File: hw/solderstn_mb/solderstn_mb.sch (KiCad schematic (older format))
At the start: 0 parts

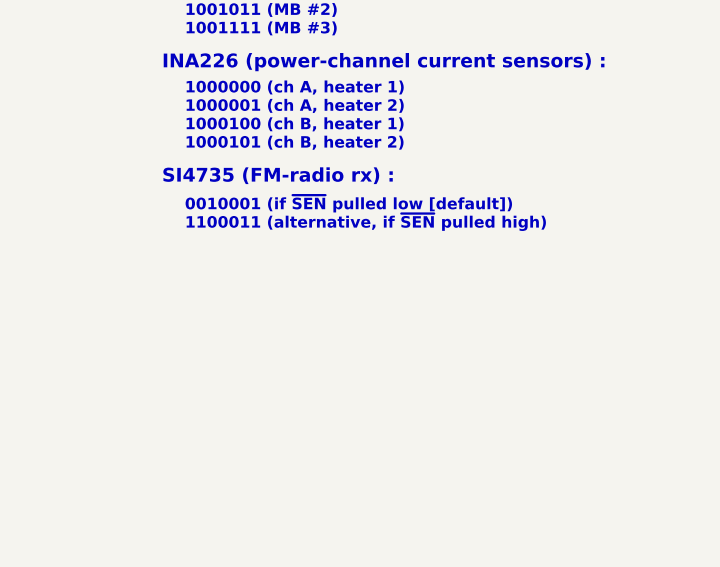
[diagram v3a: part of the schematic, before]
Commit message: Pinout changes to add DS3231 RTC module instead of 32kHz LSE xtal (still keep SMD pads as placeholders). Minor ERC fixes. All footprints specified
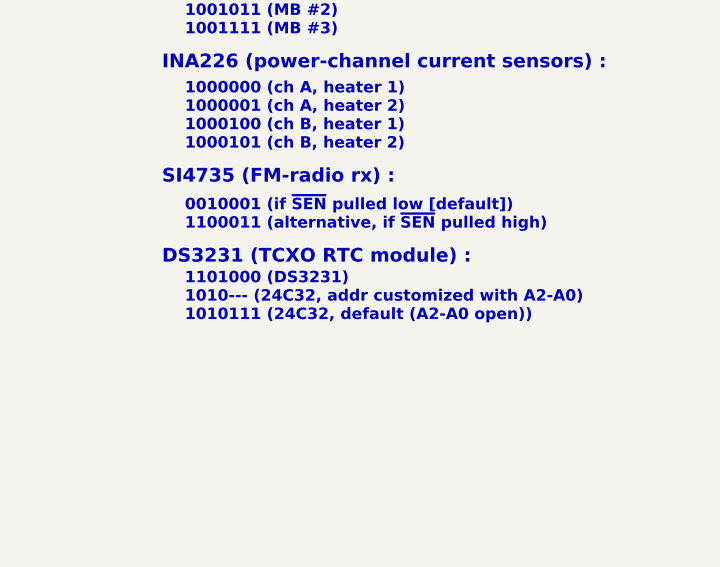
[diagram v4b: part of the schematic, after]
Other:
- note added: "1101000 (DS3231)\n1010--- (24C32, addr customized with A2-A0)\n1010111 (24C32, default (A2-A0 open))"
- note added: "DS3231 (TCXO RTC module) :"
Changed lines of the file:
@@
 Wire Wire Line
 	3400 4950 3800 4950
+Text Notes 9100 2900 0    60   ~ 12
+DS3231 (TCXO RTC module) :
+Text Notes 9200 3150 0    50   ~ 10
+1101000 (DS3231)\n1010--- (24C32, addr customized with A2-A0)\n1010111 (24C32, default (A2-A0 open))
 $EndSCHEMATC

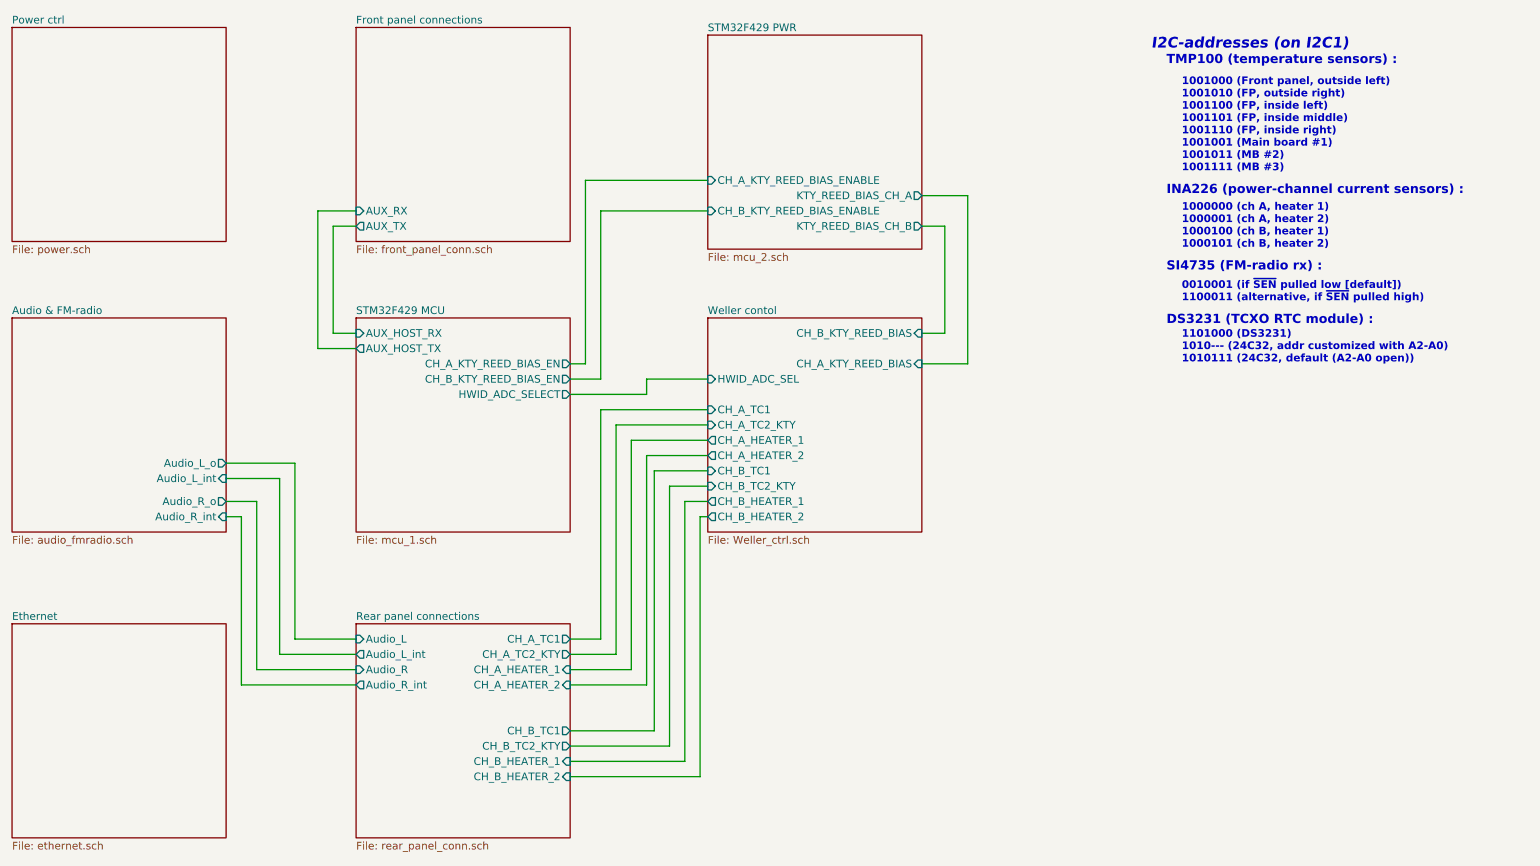
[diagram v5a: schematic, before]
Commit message: MB: moved FM-rx from audio to its own sch. sheet, to reduce clutter
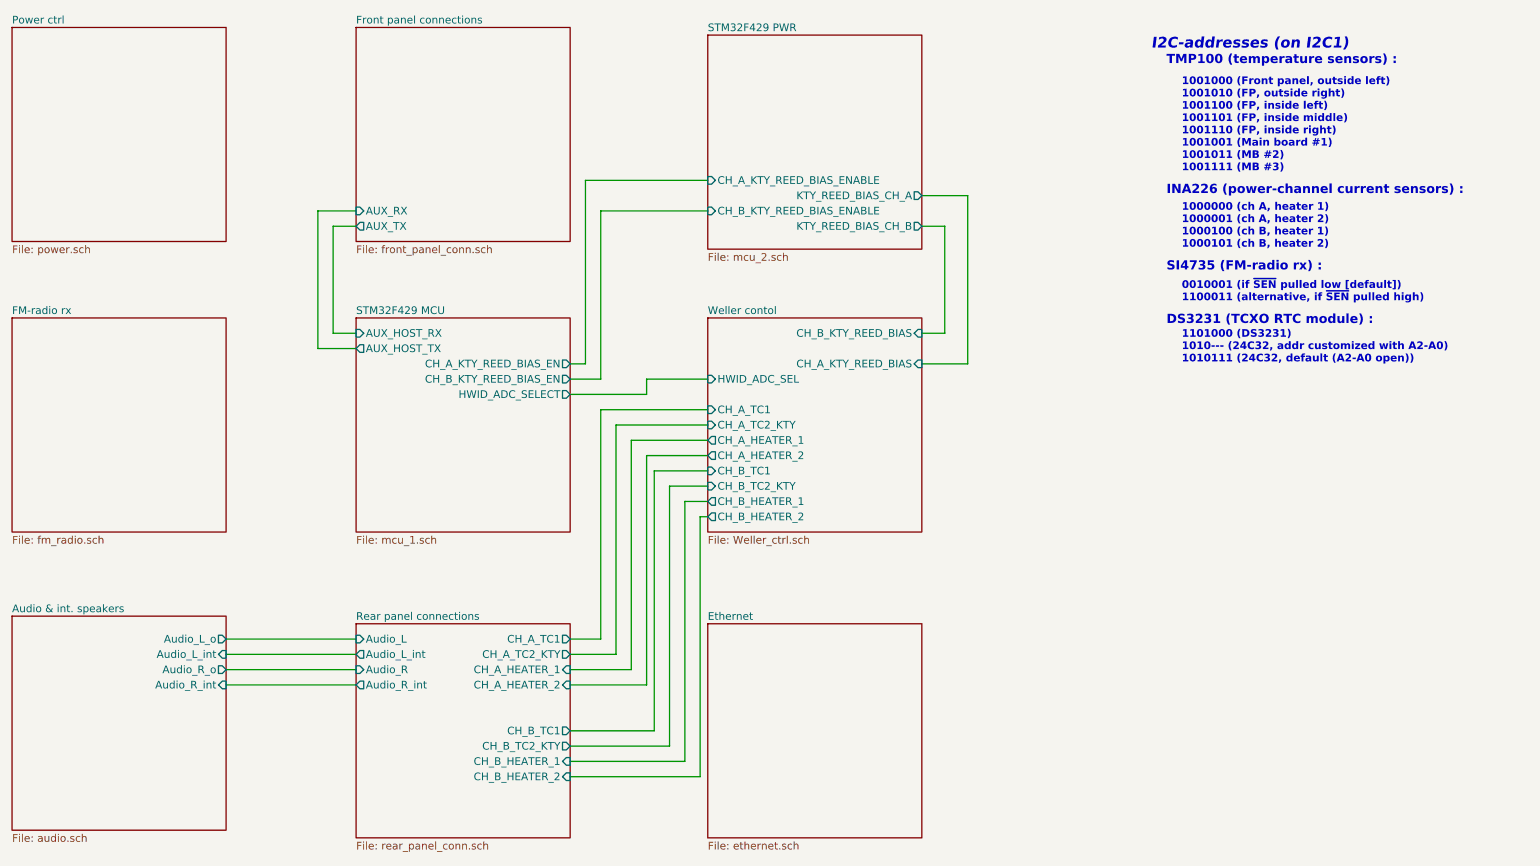
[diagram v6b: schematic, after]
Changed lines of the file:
@@
 $Descr A4 11693 8268
 encoding utf-8
-Sheet 1 21
+Sheet 1 23
 Title "DIY Soldering station, top level"
 Date "2020-04-26"
@@
 $EndDescr
 $Sheet
-S 1550 4850 1400 1400
+S 6100 4850 1400 1400
 U 5ED59CBF
 F0 "Ethernet" 50
@@
 $EndSheet
 $Sheet
-S 1550 2850 1400 1400
+S 1550 4800 1400 1400
 U 5FAFD5BA
-F0 "Audio & FM-radio" 50
-F1 "audio_fmradio.sch" 50
-F2 "Audio_R_o" O R 2950 4050 50
-F3 "Audio_L_o" O R 2950 3800 50
-F4 "Audio_R_int" I R 2950 4150 50
-F5 "Audio_L_int" I R 2950 3900 50
+F0 "Audio & int. speakers" 50
+F1 "audio.sch" 50
+F2 "Audio_R_o" O R 2950 5150 50
+F3 "Audio_L_o" O R 2950 4950 50
+F4 "Audio_R_int" I R 2950 5250 50
+F5 "Audio_L_int" I R 2950 5050 50
 $EndSheet
 $Sheet
@@
 	5700 3250 6100 3250
 Wire Wire Line
-	2950 4150 3050 4150
-Wire Wire Line
-	3050 4150 3050 5250
-Wire Wire Line
-	3050 5250 3800 5250
-Wire Wire Line
-	2950 4050 3150 4050
-Wire Wire Line
-	3150 4050 3150 5150
-Wire Wire Line
-	3150 5150 3800 5150
-Wire Wire Line
-	2950 3900 3300 3900
-Wire Wire Line
-	3300 3900 3300 5050
-Wire Wire Line
-	3300 5050 3800 5050
-Wire Wire Line
-	2950 3800 3400 3800
-Wire Wire Line
-	3400 3800 3400 4950
-Wire Wire Line
-	3400 4950 3800 4950
+	2950 5150 3800 5150
+Wire Wire Line
+	2950 5050 3800 5050
+Wire Wire Line
+	2950 4950 3800 4950
 Text Notes 9100 2900 0    60   ~ 12
 DS3231 (TCXO RTC module) :
 Text Notes 9200 3150 0    50   ~ 10
 1101000 (DS3231)\n1010--- (24C32, addr customized with A2-A0)\n1010111 (24C32, default (A2-A0 open))
+Wire Wire Line
+	2950 5250 3800 5250
+$Sheet
+S 1550 2850 1400 1400
+U 5FE3F0D8
+F0 "FM-radio rx" 50
+F1 "fm_radio.sch" 50
+$EndSheet
 $EndSCHEMATC
